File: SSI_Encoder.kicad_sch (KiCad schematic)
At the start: 36 parts, among them J2 DE9_Socket_MountingHoles, J4 DE9_Socket_MountingHoles, Q6 2N7002KQ-7, Q7 2N7002KQ-7, U16 ISO1432DWR, U22 SN74LVC2G07DCKR(UMW), U26 TPD1E10B09DPYR, U27 TPD1E10B09DPYR, U3 TPD2E2U06QDBZRQ1, U6 TPD2E2U06QDBZRQ1, U7 ISO1432DWR, U8 TPD2E2U06QDBZRQ1, U9 TPD2E2U06QDBZRQ1

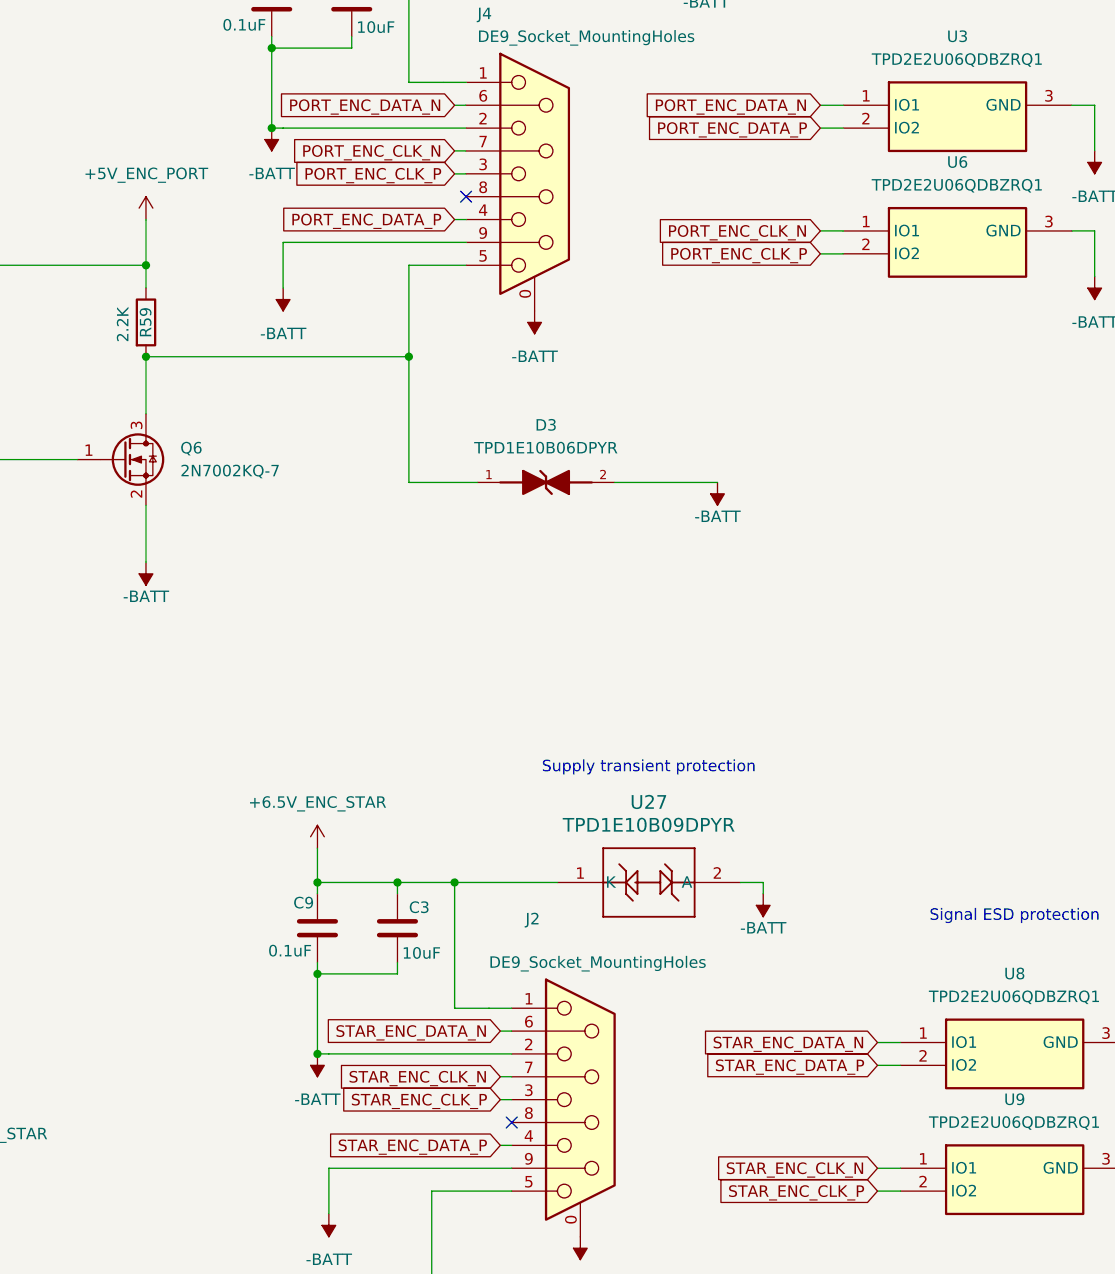
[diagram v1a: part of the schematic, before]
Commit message: Preserve P5 equal-size placement, controller stack and native BOM
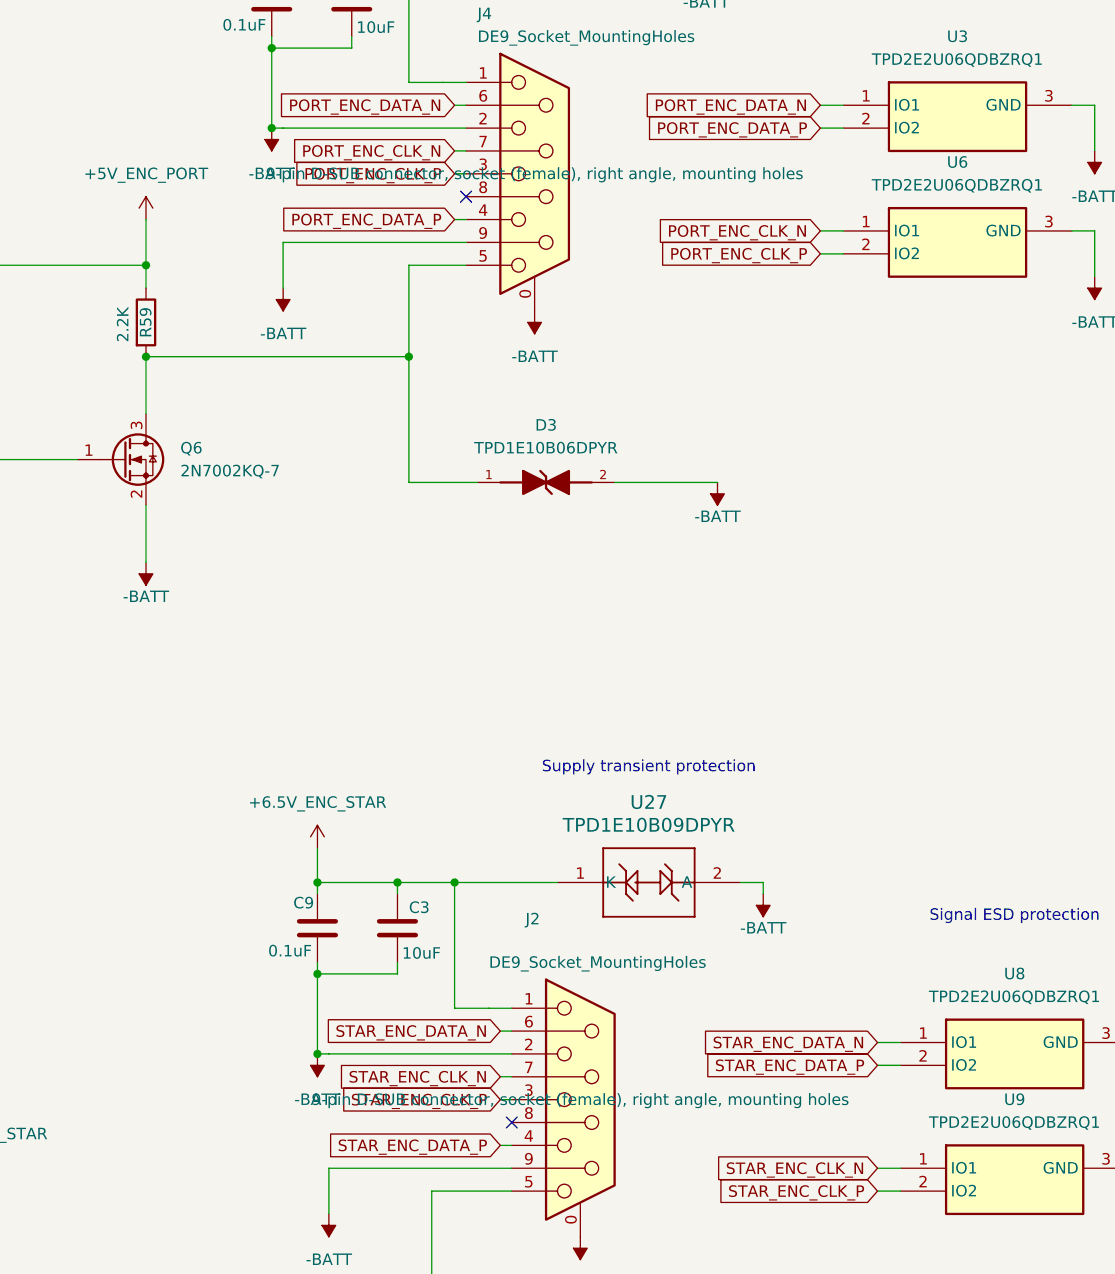
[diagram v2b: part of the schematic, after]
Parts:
- C17, C3: Assembly (none) -> FIT; BOM Status (none) -> PART IDENTIFIED; sourcing/footprint review pending; Footprint Status (none) -> Assigned; drawing/pad verification pending; Function (none) -> Unpolarized capacitor; JLCPCB Status (none) -> Historical ID; recheck exact part and assembly availability; MPN (none) -> FS55X106K101EHG; Supplier Data Checked (none) -> UNDATED legacy record; Supplier Source (none) -> Legacy schematic record; exact supplier listing verificatio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; Temp Basis (none) -> Legacy rating; ambient/junction basis unverified; Temp Max (degC) (none) -> 125; Temp Min (degC) (none) -> -55; Temp Source (none) -> Legacy schematic field; primary-source verification pending; Temp Status (none) -> Inherited rating; system requirement pending
- C2, C56, C57, C62, C65, C9, C99: Assembly (none) -> FIT; BOM Status (none) -> PART IDENTIFIED; sourcing/footprint review pending; Footprint Status (none) -> Assigned; drawing/pad verification pending; Function (none) -> Unpolarized capacitor; JLCPCB Status (none) -> Historical ID; recheck exact part and assembly availability; MPN (none) -> CL21B104KCFNNNE; Supplier Data Checked (none) -> UNDATED legacy record; Supplier Source (none) -> Legacy schematic record; exact supplier listing verificatio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; Temp Basis (none) -> Legacy rating; ambient/junction basis unverified; Temp Max (degC) (none) -> 125; Temp Min (degC) (none) -> -55; Temp Source (none) -> Legacy schematic field; primary-source verification pending; Temp Status (none) -> Inherited rating; system requirement pending
- C58, C6, C63, C64: Assembly (none) -> FIT; BOM Status (none) -> PART IDENTIFIED; sourcing/footprint review pending; Footprint Status (none) -> Assigned; drawing/pad verification pending; Function (none) -> Unpolarized capacitor; JLCPCB Status (none) -> Historical ID; recheck exact part and assembly availability; MPN (none) -> CL31B105KCHNNNE; Supplier Data Checked (none) -> UNDATED legacy record; Supplier Source (none) -> Legacy schematic record; exact supplier listing verificatio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; Temp Basis (none) -> Legacy rating; ambient/junction basis unverified; Temp Max (degC) (none) -> 125; Temp Min (degC) (none) -> -55; Temp Source (none) -> Legacy schematic field; primary-source verification pending; Temp Status (none) -> Inherited rating; system requirement pending
- D2, D3: Assembly (none) -> FIT; BOM Status (none) -> PART IDENTIFIED; sourcing/footprint review pending; Footprint Status (none) -> Assigned; drawing/pad verification pending; Function (none) -> TPD1E10B06DPYR; JLCPCB Status (none) -> Historical ID; recheck exact part and assembly availability; MPN (none) -> TPD1E10B06DPYR; Supplier Data Checked (none) -> UNDATED legacy record; Supplier Source (none) -> Legacy schematic record; exact supplier listing verificatio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; Temp Basis (none) -> Legacy rating; ambient/junction basis unverified; Temp Max (degC) (none) -> 125; Temp Min (degC) (none) -> -40; Temp Source (none) -> Legacy schematic field; primary-source verification pending; Temp Status (none) -> Inherited rating; system requirement pending
- J2, J4: Assembly (none) -> FIT; BOM Review (none) -> Same MPN as existing DE9 connectors. Verify exact pin grid,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; BOM Status (none) -> PART IDENTIFIED; sourcing/footprint review pending; Footprint Status (none) -> REVIEW: compare exact TE drawing to generic KiCad footprint; Function (none) -> DE9 female right-angle PCB connector; JLCPCB Library (none) -> UNVERIFIED; JLCPCB Status (none) -> LCSC exact match; JLC assembly availability unverified; MPN (none) -> 5747844-4; Supplier Data Checked (none) -> 2026-10-03; Supplier Source (none) -> https://www.lcsc.com/de/product-detail/C305941.html; Temp Basis (none) -> Operating; Temp Checked (none) -> 2026-10-03; Temp Max (degC) (none) -> 105; Temp Min (degC) (none) -> -55; Temp Source (none) -> https://www.te.com/en/product-5747844-4.html; Temp Status (none) -> Manufacturer rating recorded; system requirement pending
- Q6, Q7: Assembly (none) -> FIT; BOM Review (none) -> Legacy datasheet points to onsemi NDS7002A rather than sele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; BOM Status (none) -> REVIEW: legacy datasheet/manufacturer mismatch; Footprint Status (none) -> Assigned; drawing/pad verification pending; Function (none) -> 0.115A Id, 60V Vds, N-Channel MOSFET, SOT-23; JLCPCB Status (none) -> Historical ID; recheck exact part and assembly availability; MPN (none) -> 2N7002KQ-7; Supplier Data Checked (none) -> UNDATED legacy record; Supplier Source (none) -> Legacy schematic record; exact supplier listing verificatio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; Temp Basis (none) -> Legacy rating; ambient/junction basis unverified; Temp Max (degC) (none) -> 150; Temp Min (degC) (none) -> -55; Temp Source (none) -> Legacy schematic field; primary-source verification pending; Temp Status (none) -> Legacy rating unverified; exact manufacturer datasheet requ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
- R2, R4: Assembly (none) -> FIT; BOM Status (none) -> PART IDENTIFIED; sourcing/footprint review pending; Footprint Status (none) -> Assigned; drawing/pad verification pending; Function (none) -> Resistor; JLCPCB Status (none) -> Historical ID; recheck exact part and assembly availability; MPN (none) -> RC0805FR-07120RL; Supplier Data Checked (none) -> UNDATED legacy record; Supplier Source (none) -> Legacy schematic record; exact supplier listing verificatio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; Temp Basis (none) -> Legacy rating; ambient/junction basis unverified; Temp Max (degC) (none) -> 155; Temp Min (degC) (none) -> -55; Temp Source (none) -> Legacy schematic field; primary-source verification pending; Temp Status (none) -> Inherited rating; system requirement pending
- R39, R40: Assembly (none) -> FIT; BOM Status (none) -> PART IDENTIFIED; sourcing/footprint review pending; Footprint Status (none) -> Assigned; drawing/pad verification pending; Function (none) -> Resistor; JLCPCB Status (none) -> Historical ID; recheck exact part and assembly availability; MPN (none) -> RC0805FR-0710KL; Supplier Data Checked (none) -> UNDATED legacy record; Supplier Source (none) -> Legacy schematic record; exact supplier listing verificatio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; Temp Basis (none) -> Legacy rating; ambient/junction basis unverified; Temp Max (degC) (none) -> 155; Temp Min (degC) (none) -> -55; Temp Source (none) -> Legacy schematic field; primary-source verification pending; Temp Status (none) -> Inherited rating; system requirement pending
- R59, R60: Assembly (none) -> FIT; BOM Status (none) -> PART IDENTIFIED; sourcing/footprint review pending; Footprint Status (none) -> Assigned; drawing/pad verification pending; Function (none) -> Resistor; JLCPCB Status (none) -> Historical ID; recheck exact part and assembly availability; MPN (none) -> RC0805FR-072K2L; Supplier Data Checked (none) -> UNDATED legacy record; Supplier Source (none) -> Legacy schematic record; exact supplier listing verificatio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; Temp Basis (none) -> Legacy rating; ambient/junction basis unverified; Temp Max (degC) (none) -> 155; Temp Min (degC) (none) -> -55; Temp Source (none) -> Legacy schematic field; primary-source verification pending; Temp Status (none) -> Inherited rating; system requirement pending
- R61, R62: Assembly (none) -> FIT; BOM Status (none) -> PART IDENTIFIED; sourcing/footprint review pending; Footprint Status (none) -> Assigned; drawing/pad verification pending; Function (none) -> Resistor; JLCPCB Status (none) -> Historical ID; recheck exact part and assembly availability; MPN (none) -> RC0805FR-0747KL; Supplier Data Checked (none) -> UNDATED legacy record; Supplier Source (none) -> Legacy schematic record; exact supplier listing verificatio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; Temp Basis (none) -> Legacy rating; ambient/junction basis unverified; Temp Max (degC) (none) -> 155; Temp Min (degC) (none) -> -55; Temp Source (none) -> Legacy schematic field; primary-source verification pending; Temp Status (none) -> Inherited rating; system requirement pending
- U16, U7: Assembly (none) -> FIT; BOM Status (none) -> PART IDENTIFIED; sourcing/footprint review pending; Footprint Status (none) -> Assigned; drawing/pad verification pending; Function (none) -> ISO1432DWR; JLCPCB Status (none) -> Historical ID; recheck exact part and assembly availability; MPN (none) -> ISO1432DWR; Supplier Data Checked (none) -> UNDATED legacy record; Supplier Source (none) -> Legacy schematic record; exact supplier listing verificatio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; Temp Basis (none) -> Legacy rating; ambient/junction basis unverified; Temp Max (degC) (none) -> 125; Temp Min (degC) (none) -> -40; Temp Source (none) -> Legacy schematic field; primary-source verification pending; Temp Status (none) -> Inherited rating; system requirement pending
- U22: Assembly (none) -> FIT; BOM Status (none) -> PART IDENTIFIED; sourcing/footprint review pending; Footprint Status (none) -> Assigned; drawing/pad verification pending; Function (none) -> SN74LVC2G07DCKR(UMW); JLCPCB Status (none) -> Historical ID; recheck exact part and assembly availability; MPN (none) -> SN74LVC2G07DCKR(UMW); Supplier Data Checked (none) -> UNDATED legacy record; Supplier Source (none) -> Legacy schematic record; exact supplier listing verificatio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; Temp Basis (none) -> Legacy rating; ambient/junction basis unverified; Temp Max (degC) (none) -> 125; Temp Min (degC) (none) -> -55; Temp Source (none) -> Legacy schematic field; primary-source verification pending; Temp Status (none) -> Inherited rating; system requirement pending
- U26, U27: Assembly (none) -> FIT; BOM Status (none) -> PART IDENTIFIED; sourcing/footprint review pending; Footprint Status (none) -> Assigned; drawing/pad verification pending; Function (none) -> TPD1E10B09DPYR; JLCPCB Status (none) -> Historical ID; recheck exact part and assembly availability; MPN (none) -> TPD1E10B09DPYR; Supplier Data Checked (none) -> UNDATED legacy record; Supplier Source (none) -> Legacy schematic record; exact supplier listing verificatio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; Temp Basis (none) -> Legacy rating; ambient/junction basis unverified; Temp Max (degC) (none) -> 125; Temp Min (degC) (none) -> -40; Temp Source (none) -> Legacy schematic field; primary-source verification pending; Temp Status (none) -> Inherited rating; system requirement pending
- U3, U6, U8, U9: Assembly (none) -> FIT; BOM Status (none) -> PART IDENTIFIED; sourcing/footprint review pending; Footprint Status (none) -> Assigned; drawing/pad verification pending; Function (none) -> Automotive Dual-Channel High-Speed ESD Protection Device; JLCPCB Status (none) -> Historical ID; recheck exact part and assembly availability; MPN (none) -> TPD2E2U06QDBZRQ1; Supplier Data Checked (none) -> UNDATED legacy record; Supplier Source (none) -> Legacy schematic record; exact supplier listing verificatio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; Temp Basis (none) -> Legacy rating; ambient/junction basis unverified; Temp Max (degC) (none) -> 125; Temp Min (degC) (none) -> -40; Temp Source (none) -> Legacy schematic field; primary-source verification pending; Temp Status (none) -> Inherited rating; system requirement pending
